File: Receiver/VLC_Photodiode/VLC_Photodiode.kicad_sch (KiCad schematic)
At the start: 7 parts, among them J1 Screw_Terminal_01x02, J2 RF3-05-T-00-50-G, J3 RF3-05-T-00-50-G, J4 RF3-05-T-00-50-G

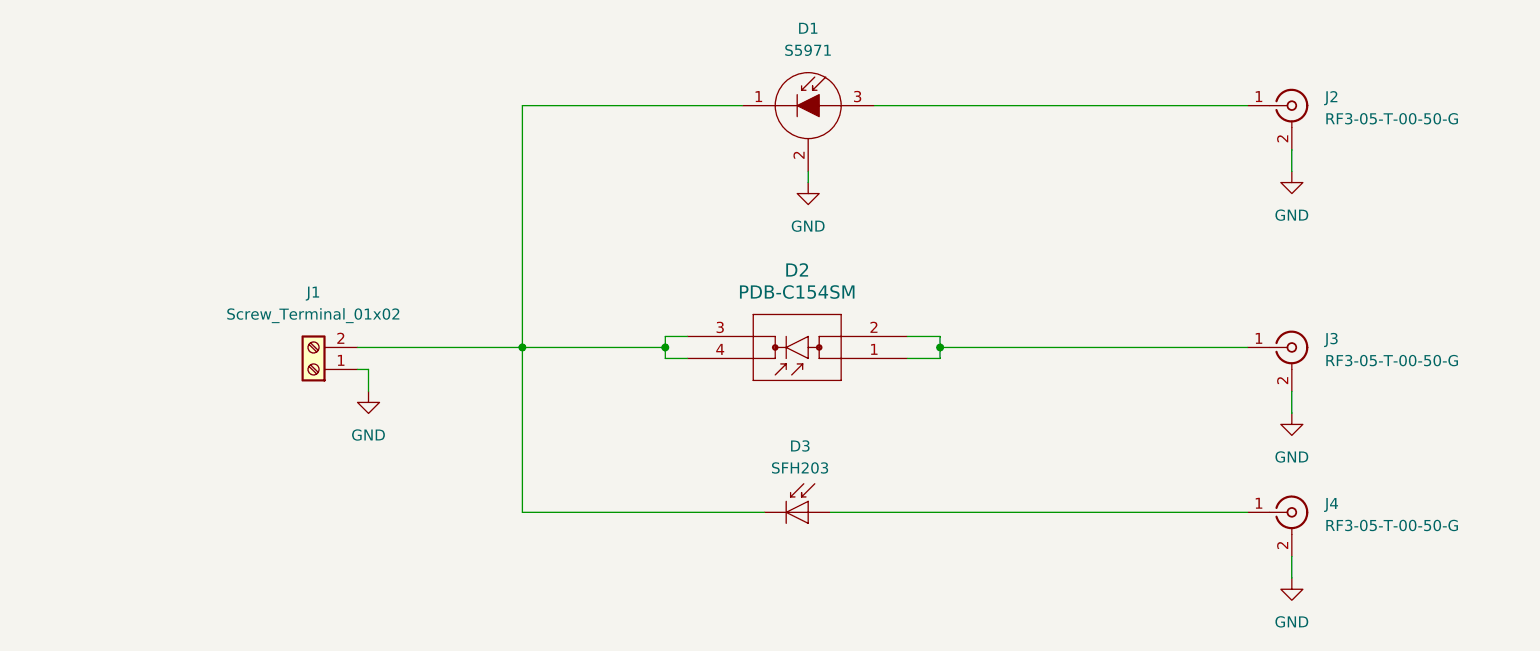
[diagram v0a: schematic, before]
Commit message: Push v2 according to Issue#1
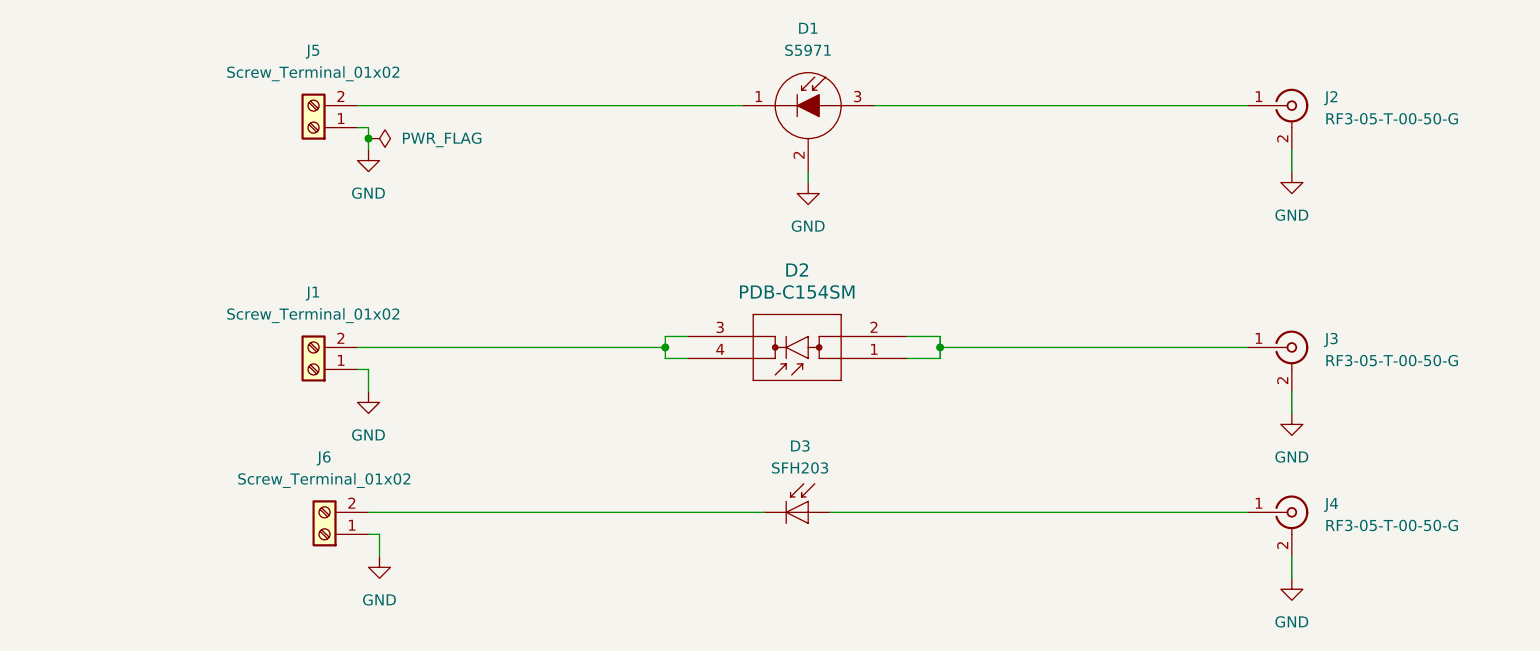
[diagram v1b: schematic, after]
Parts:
- added J5, J6: Screw_Terminal_01x02, TerminalBlock:TerminalBlock_bornier-2_P5.08mm, symbol Connector:Screw_Terminal_01x02
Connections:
- net GND: now also J5.1 (Pin_1), J6.1 (Pin_1)
- net at D2.3 (CATHODE), D2.4 (CATHODE), J1.2 (Pin_2): no longer D1.1 (K), D3.1 (K)
- new net: D3.1 (K), J6.2 (Pin_2)
- new net: D1.1 (K), J5.2 (Pin_2)

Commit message: Version Sma Edge
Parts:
- J2, J3, J4: value RF3-05-T-00-50-G -> SMA H; footprint Lumicom_Photodiode:RF305T0050G -> Connector_Coaxial:SMA_Samtec_SMA-J-P-H-ST-EM1_EdgeMount
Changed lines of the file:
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@@
 			)
 		)
-		(property "Value" "RF3-05-T-00-50-G"
+		(property "Value" "SMA H"
 			(at 201.93 72.6831 0)
 			(effects
@@
 			)
 		)
-		(property "Footprint" "Lumicom_Photodiode:RF305T0050G"
+		(property "Footprint" "Connector_Coaxial:SMA_Samtec_SMA-J-P-H-ST-EM1_EdgeMount"
 			(at 198.12 71.12 0)
 			(effects
@@
 			)
 		)
-		(property "Value" "RF3-05-T-00-50-G"
+		(property "Value" "SMA H"
 			(at 201.93 100.6231 0)
 			(effects
@@
 			)
 		)
-		(property "Footprint" "Lumicom_Photodiode:RF305T0050G"
+		(property "Footprint" "Connector_Coaxial:SMA_Samtec_SMA-J-P-H-ST-EM1_EdgeMount"
 			(at 198.12 99.06 0)
 			(effects
@@
 	)
 	(symbol
+		(lib_id "power:GND")
+		(at 142.24 80.01 0)
+		(unit 1)
+		(exclude_from_sim no)
+		(in_bom yes)
+		(on_board yes)
+		(dnp no)
+		(fields_autoplaced yes)
+		(property "Reference" "#PWR07"
+			(at 142.24 86.36 0)
+			(effects
+				(font
+					(size 1.27 1.27)
+				)
+				(hide yes)
+			)
+		)
+		(property "Value" "GND"
+			(at 142.24 85.09 0)
+			(effects
+				(font
+					(size 1.27 1.27)
+				)
+			)
+		)
+		(property "Footprint" ""
+			(at 142.24 80.01 0)
+			(effects
+				(font
+					(size 1.27 1.27)
+				)
+				(hide yes)
+			)
+		)
+		(property "Datasheet" ""
+			(at 142.24 80.01 0)
+			(effects
+				(font
+					(size 1.27 1.27)
+				)
+				(hide yes)
+			)
+		)
+		(property "Description" "Power symbol creates a global label with name \"GND\" , ground"
+			(at 142.24 80.01 0)
+			(effects
+				(font
+					(size 1.27 1.27)
+				)
+				(hide yes)
+			)
+		)
+		(pin "1"
+		)
+		(instances
+			(project "VLC_Photodiode"
+				(path "/43100d71-c391-405d-9a3f-a9fcd4b54745"
+					(reference "#PWR07")
+					(unit 1)
+				)
+			)
+		)
+	)
+	(symbol
 		(lib_id "Connector:Conn_Coaxial")
 		(at 198.12 118.11 0)
@@
 			)
 		)
-		(property "Value" "RF3-05-T-00-50-G"
+		(property "Value" "SMA H"
 			(at 201.93 119.6731 0)
 			(effects
@@
 			)
 		)
-		(property "Footprint" "Lumicom_Photodiode:RF305T0050G"
+		(property "Footprint" "Connector_Coaxial:SMA_Samtec_SMA-J-P-H-ST-EM1_EdgeMount"
 			(at 198.12 118.11 0)
 			(effects
@@
 					(unit 1)
 				)
-			)
-		)
-	)
-	(symbol
-		(lib_id "power:GND")
-		(at 142.24 80.01 0)
-		(unit 1)
-		(exclude_from_sim no)
-		(in_bom yes)
-		(on_board yes)
-		(dnp no)
-		(fields_autoplaced yes)
-		(property "Reference" "#PWR07"
-			(at 142.24 86.36 0)
-			(effects
-				(font
-					(size 1.27 1.27)
-				)
-				(hide yes)
-			)
-		)
-		(property "Value" "GND"
-			(at 142.24 85.09 0)
-			(effects
-				(font
-					(size 1.27 1.27)
-				)
-			)
-		)
-		(property "Footprint" ""
-			(at 142.24 80.01 0)
-			(effects
-				(font
-					(size 1.27 1.27)
-				)
-				(hide yes)
-			)
-		)
-		(property "Datasheet" ""
-			(at 142.24 80.01 0)
-			(effects
-				(font
-					(size 1.27 1.27)
-				)
-				(hide yes)
-			)
-		)
-		(property "Description" "Power symbol creates a global label with name \"GND\" , ground"
-			(at 142.24 80.01 0)
-			(effects
-				(font
-					(size 1.27 1.27)
-				)
-				(hide yes)
-			)
-		)
-		(pin "1"
-		)
-		(instances
-			(project "VLC_Photodiode"
-				(path "/43100d71-c391-405d-9a3f-a9fcd4b54745"
-					(reference "#PWR07")
-					(unit 1)
-				)

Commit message: v3 according to Issue #1
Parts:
- D1: Mfr (none) -> Hamamatsu; Mfr P/N (none) -> S5971; Newark P/N (none) -> 62M0262
- D2: Mfr (none) -> Advanced Photonix; Mfr P/N (none) -> PDB-C154SM; Mouser P/N (none) -> 846-PDB-C154SM
- D3: Mfr (none) -> ams OSRAM; Mfr P/N (none) -> SFH 203 P; Mouser P/N (none) -> 720-SFH203P
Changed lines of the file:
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@@
 			)
 		)
-		(property "Datasheet" "http://www.osram-os.com/Graphics/XPic9/00101656_0.pdf/SFH%20203,%20SFH%20203%20FA,%20Lead%20(Pb)%20Free%20Product%20-%20RoHS%20Compliant.pdf"
+		(property "Datasheet" "https://ar.mouser.com/datasheet/2/588/asset_pdf_5174114-3419302.pdf"
 			(at 140.97 118.11 0)
 			(effects
@@
 			)
 		)
+		(property "Mfr P/N" "SFH 203 P"
+			(at 142.24 118.11 0)
+			(effects
+				(font
+					(size 1.27 1.27)
+				)
+				(hide yes)
+			)
+		)
+		(property "Mouser P/N" "720-SFH203P"
+			(at 142.24 118.11 0)
+			(effects
+				(font
+					(size 1.27 1.27)
+				)
+				(hide yes)
+			)
+		)
+		(property "Mfr" "ams OSRAM"
+			(at 142.24 118.11 0)
+			(effects
+				(font
+					(size 1.27 1.27)
+				)
+				(hide yes)
+			)
+		)
 		(pin "2"
 		)
@@
 			)
 		)
-		(property "Datasheet" "PDB-C154SM"
+		(property "Datasheet" "https://www.advancedphotonix.com/wp-content/uploads/2022/03/DS-PDB-C154SM.pdf"
 			(at 140.462 93.726 0)
 			(effects
@@
 			)
 		)
+		(property "Mfr P/N" "PDB-C154SM"
+			(at 152.4 100.33 0)
+			(effects
+				(font
+					(size 1.27 1.27)
+				)
+				(hide yes)
+			)
+		)
+		(property "Mouser P/N" "846-PDB-C154SM"
+			(at 152.4 100.33 0)
+			(effects
+				(font
+					(size 1.27 1.27)
+				)
+				(hide yes)
+			)
+		)
+		(property "Mfr" "Advanced Photonix"
+			(at 152.4 100.33 0)
+			(effects
+				(font
+					(size 1.27 1.27)
+				)
+				(hide yes)
+			)
+		)
 		(pin "3"
 		)
@@
 			(at 142.24 71.12 0)
 			(effects
+				(font
+					(size 1.27 1.27)
+				)
+				(hide yes)
+			)
+		)
+		(property "Mfr P/N" " S5971"
+			(at 142.24 71.12 0)
+			(effects
+				(font
+					(size 1.27 1.27)
+				)
+				(hide yes)
+			)
+		)
+		(property "Newark P/N" "62M0262"
+			(at 142.24 71.12 0)
+			(effects
+				(font
+					(size 1.27 1.27)
+				)
+				(hide yes)
+			)
+		)
+		(property "Mfr" "Hamamatsu"
+			(at 142.24 71.12 0)
+			(effects

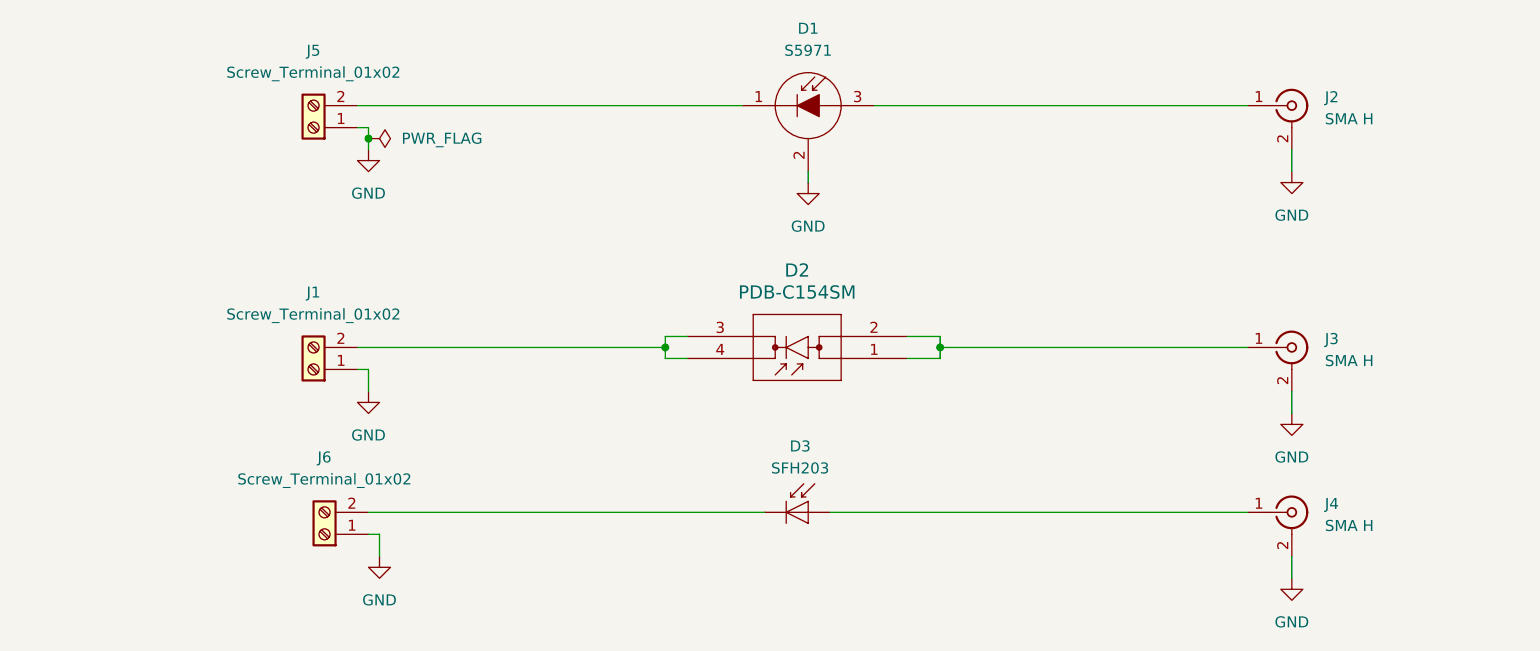
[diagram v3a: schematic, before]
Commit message: LED uploaded, PD reworked
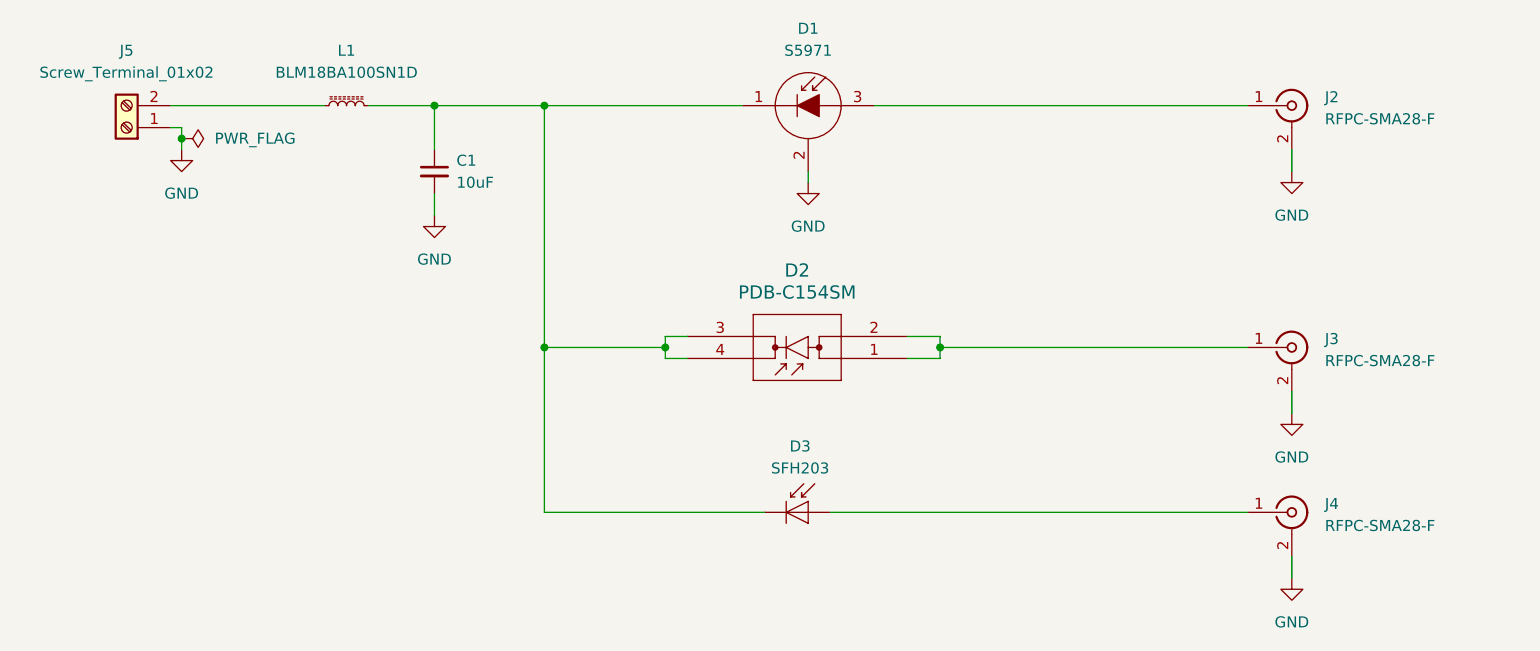
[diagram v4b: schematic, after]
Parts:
- removed J1, J6: Screw_Terminal_01x02, TerminalBlock:TerminalBlock_bornier-2_P5.08mm, symbol Connector:Screw_Terminal_01x02
- added C1: 10uF, Capacitor_SMD:C_0603_1608Metric_Pad1.08x0.95mm_HandSolder, symbol Device:C_Small
- added L1: BLM18BA100SN1D, Inductor_SMD:L_0603_1608Metric_Pad1.05x0.95mm_HandSolder, symbol Device:L_Ferrite_Small
- J2, J3, J4: value SMA H -> RFPC-SMA28-F; footprint Connector_Coaxial:SMA_Samtec_SMA-J-P-H-ST-EM1_EdgeMount -> Lumicom_Photodiode:RFPC-SMA28-F
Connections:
- net GND: now also C1.2
- net at D3.1 (K): now also D1.1 (K), D2.3 (CATHODE), D2.4 (CATHODE), C1.1, L1.2
- net at J5.2 (Pin_2): now also L1.1; no longer D1.1 (K)
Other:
- moved on the sheet: J5
